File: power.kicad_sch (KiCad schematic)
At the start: 51 parts, among them CN8 POWER, U1 68000D, U10 74LS244, U11 74LS373, U12 74LS244, U13 74LS373, U2 FAT_AGNUS_8375, U32 74LS139, U34 74LS244, U35 74LS244, U36 74LS05, U37 74LS32, U5 GARY_5719, X1 XTAL

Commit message: Working on BOM
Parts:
- C1, C11, C13, C14, C2, C5, C804: MFG Part Num C412C334M5U5TA -> C440C334K5R5TA7200; Mouser (none) -> 80-C440C334K5R-TR
- C10, C12, C32, C34, C35, C36, C37, C701, C800, C801, C802, C803: MFG Part Num C410C103K1H5TAAUTO -> C410C103K1R5TA; Mouser (none) -> 80-C410C103K1R
- C811, C812, C813, C814, C815, C816: MFG Part Num EEUFR1H101 -> ECA-1VM101B; Mouser (none) -> 667-ECA-1VM101B
- C821, C822: MFG Part Num EEUFR1H470 -> ECA-1VM470B; Mouser (none) -> 667-ECA-1VM470B
- CN8: MFG Name (none) -> COMMODORE; MFG Part Num (none) -> 252167-01

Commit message: more work on BOM done
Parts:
- E101, E110: Mouser (none) -> 81-DSS1NB32A103Q91A
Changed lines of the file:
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@@
 			)
 		)
-		(property "Mouser" ""
+		(property "Mouser" " 81-DSS1NB32A103Q91A "
 			(at 109.728 104.394 90)
 			(effects
@@
 			)
 		)
-		(property "Mouser" ""
+		(property "Mouser" " 81-DSS1NB32A103Q91A "
 			(at 146.558 104.394 90)
 			(effects

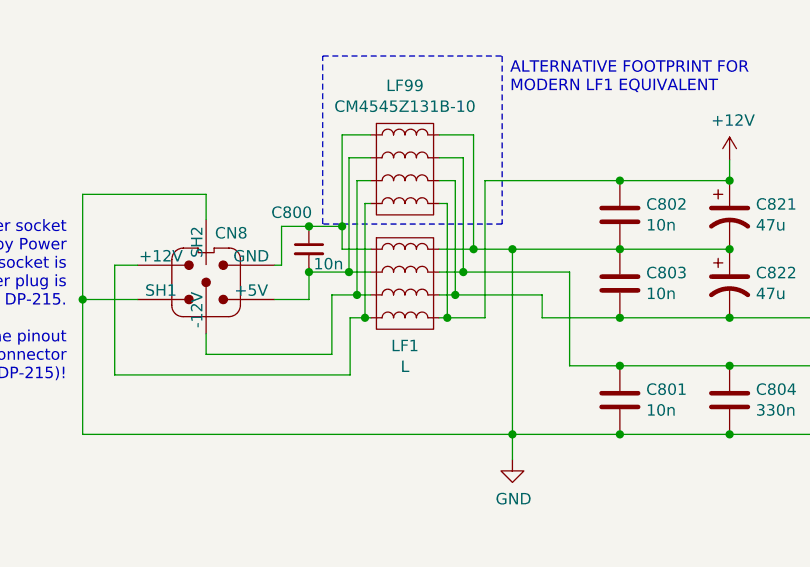
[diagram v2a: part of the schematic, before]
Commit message: More BOM work
I am marking optional components as DNP to get some overview
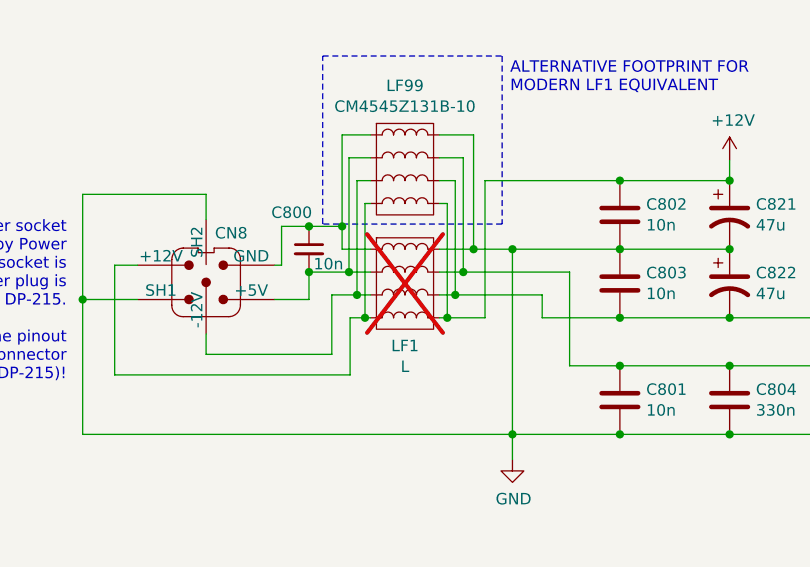
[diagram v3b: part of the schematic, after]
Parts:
- E101, E110: Mouser 81-DSS1NB32A103Q91A -> 81-DSS1NB32A103Q91A
- LF1: MFG Name (none) -> COMMODORE; now not fitted
- LF99: MFG Name (none) -> LAIRD; MFG Part Num (none) -> CM4545Z131B-10; Mouser (none) -> 875-CM4545Z131B-10
- U1: MFG Name (none) -> MOTOROLA
- U2, U5: MFG Name (none) -> COMMODORE
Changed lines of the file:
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@@
 		(in_bom yes)
 		(on_board yes)
-		(dnp no)
+		(dnp yes)
 		(property "Reference" "LF1"
 			(at 93.726 63.4492 0)
@@
 			)
 		)
+		(property "MFG Name" "COMMODORE"
+			(at 93.726 56.515 0)
+			(effects
+				(font
+					(size 1.27 1.27)
+				)
+				(hide yes)
+			)
+		)
 		(pin "4"
 		)
@@
 			)
 		)
+		(property "MFG Name" "COMMODORE"
+			(at 184.658 128.524 0)
+			(effects
+				(font
+					(size 1.27 1.27)
+				)
+				(hide yes)
+			)
+		)
 		(pin "34"
 		)
@@
 			)
 		)
+		(property "MFG Name" "MOTOROLA"
+			(at 74.168 129.794 0)
+			(effects
+				(font
+					(size 1.27 1.27)
+				)
+				(hide yes)
+			)
+		)
 		(pin "20"
 		)
@@
 			)
 		)
+		(property "MFG Name" "COMMODORE"
+			(at 112.268 127.254 0)
+			(effects
+				(font
+					(size 1.27 1.27)
+				)
+				(hide yes)
+			)
+		)
 		(pin "59"
 		)
@@
 			)
 		)
-		(property "Mouser" " 81-DSS1NB32A103Q91A "
+		(property "Mouser" "81-DSS1NB32A103Q91A "
 			(at 109.728 104.394 90)
 			(effects
@@
 			)
 		)
-		(property "Mouser" " 81-DSS1NB32A103Q91A "
+		(property "Mouser" "81-DSS1NB32A103Q91A "
 			(at 146.558 104.394 90)
 			(effects
@@
 			)
 		)
-		(property "Mouser" ""
+		(property "Mouser" "875-CM4545Z131B-10 "
+			(at 93.726 43.815 0)
+			(effects
+				(font
+					(size 1.27 1.27)
+				)
+				(hide yes)
+			)
+		)
+		(property "MFG Name" "LAIRD"
+			(at 93.726 43.815 0)
+			(effects
+				(font
+					(size 1.27 1.27)
+				)
+				(hide yes)
+			)
+		)
+		(property "MFG Part Num" "CM4545Z131B-10"
 			(at 93.726 43.815 0)
 			(effects

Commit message: BOM updates
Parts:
- U1: MFG Name MOTOROLA -> MILL-MAX; MFG Part Num (none) -> 110-93-964-41-001000; Mouser (none) -> 575-193964
- U10, U12, U35: MFG Part Num SN74LS244N -> SN74LS244N; Mouser (none) -> 595-SN74LS244N
- U11, U13: Mouser (none) -> 595-SN74LS373N
- U2: MFG Name COMMODORE -> MILL-MAX; MFG Part Num (none) -> 940-44-084-24-000000; Mouser (none) -> 575-948424
- U32: MFG Part Num SN74LS139AN -> SN74LS139AN; Mouser (none) -> 595-SN74LS139AN
- U34: MFG Name (none) -> TI; MFG Part Num (none) -> SN74LS244N; Mouser (none) -> 595-SN74LS244N
- U36: MFG Part Num SN74LS05N -> SN74LS05N; Mouser (none) -> 595-SN74LS05N
- U37: MFG Part Num SN74LS32N -> SN74LS32N; Mouser (none) -> 595-SN74LS32N
- U5: MFG Name COMMODORE -> 3M; MFG Part Num (none) -> 4848-6000-CP; Mouser (none) -> 517-4848-6000-CP
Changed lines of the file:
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@@
 			)
 		)
-		(property "MFG Part Num" "SN74LS32N"
+		(property "MFG Part Num" "SN74LS32N "
 			(at 217.678 179.324 0)
 			(effects
@@
 			)
 		)
-		(property "Mouser" ""
+		(property "Mouser" "595-SN74LS32N "
 			(at 217.678 179.324 0)
 			(effects
@@
 			)
 		)
-		(property "Mouser" ""
+		(property "Mouser" "517-4848-6000-CP "
+			(at 184.658 128.524 0)
+			(effects
+				(font
+					(size 1.27 1.27)
+				)
+				(hide yes)
+			)
+		)
+		(property "MFG Name" "3M"
 			(at 184.658 128.524 0)
 			(effects
@@
 			)
 		)
-		(property "MFG Name" "COMMODORE"
+		(property "MFG Part Num" "4848-6000-CP "
 			(at 184.658 128.524 0)
 			(effects
@@
 			)
 		)
-		(property "Mouser" ""
+		(property "Mouser" "575-193964 "
 			(at 74.168 129.794 0)
 			(effects
@@
 			)
 		)
-		(property "MFG Name" "MOTOROLA"
+		(property "MFG Name" "MILL-MAX"
+			(at 74.168 129.794 0)
+			(effects
+				(font
+					(size 1.27 1.27)
+				)
+				(hide yes)
+			)
+		)
+		(property "MFG Part Num" "110-93-964-41-001000"
 			(at 74.168 129.794 0)
 			(effects
@@
 			)
 		)
-		(property "Mouser" ""
+		(property "Mouser" "575-948424 "
 			(at 112.268 127.254 0)
 			(effects
@@
 			)
 		)
-		(property "MFG Name" "COMMODORE"
+		(property "MFG Name" "MILL-MAX"
+			(at 112.268 127.254 0)
+			(effects
+				(font
+					(size 1.27 1.27)
+				)
+				(hide yes)
+			)
+		)
+		(property "MFG Part Num" "940-44-084-24-000000 "
 			(at 112.268 127.254 0)
 			(effects
@@
 			)
 		)
-		(property "Mouser" ""
+		(property "Mouser" "595-SN74LS373N "
 			(at 72.898 236.474 0)
 			(effects
@@
 			)
 		)
-		(property "Mouser" ""
+		(property "Mouser" "595-SN74LS373N "
 			(at 145.288 236.474 0)
 			(effects
@@
 			)
 		)
-		(property "MFG Part Num" "SN74LS244N"
+		(property "MFG Part Num" "SN74LS244N "
 			(at 34.798 235.204 0)
 			(effects
@@
 			)
 		)
-		(property "Mouser" ""
+		(property "Mouser" "595-SN74LS244N "
 			(at 34.798 235.204 0)
 			(effects
@@
 			)
 		)
-		(property "MFG Part Num" "SN74LS244N"
+		(property "MFG Part Num" "SN74LS244N "
 			(at 107.188 235.204 0)
 			(effects
@@
 			)
 		)
-		(property "Mouser" ""
+		(property "Mouser" "595-SN74LS244N "
 			(at 107.188 235.204 0)
 			(effects
@@
 			)
 		)
-		(property "MFG Part Num" "SN74LS139AN"
+		(property "MFG Part Num" "SN74LS139AN "
 			(at 58.928 179.324 0)
 			(effects
@@
 			)
 		)
-		(property "Mouser" ""
+		(property "Mouser" "595-SN74LS139AN "
 			(at 58.928 179.324 0)
 			(effects
@@
 			)
 		)
-		(property "MFG Part Num" "SN74LS244N"
+		(property "MFG Part Num" "SN74LS244N "
 			(at 133.858 179.324 0)
 			(effects
@@
 			)
 		)
-		(property "Mouser" ""
+		(property "Mouser" "595-SN74LS244N "
 			(at 133.858 179.324 0)
 			(effects
@@
 			)
 		)
-		(property "MFG Part Num" "SN74LS05N"
+		(property "MFG Part Num" "SN74LS05N "
 			(at 174.498 179.324 0)
 			(effects
@@
 			)
 		)
-		(property "Mouser" ""
+		(property "Mouser" "595-SN74LS05N "
 			(at 174.498 179.324 0)
 			(effects
@@
 			)
 		)
-		(property "Mouser" ""
+		(property "Mouser" "595-SN74LS244N "
+			(at 97.028 179.324 0)
+			(effects
+				(font
+					(size 1.27 1.27)
+				)
+				(hide yes)
+			)
+		)
+		(property "MFG Name" "TI"
+			(at 97.028 179.324 0)
+			(effects
+				(font
+					(size 1.27 1.27)
+				)
+				(hide yes)
+			)
+		)
+		(property "MFG Part Num" "SN74LS244N "
 			(at 97.028 179.324 0)
 			(effects

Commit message: even  more BOM work
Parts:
- U32: value 74LS139 -> 74F139; MFG Part Num SN74LS139AN -> CD74ACT139E; Mouser 595-SN74LS139AN -> 595-CD74ACT139E
- U34, U35: value 74LS244 -> 74F244; MFG Part Num SN74LS244N -> (none); Mouser 595-SN74LS244N -> (none)
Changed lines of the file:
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@@
 			)
 		)
-		(property "Value" "74LS139"
+		(property "Value" "74F139"
 			(at 61.468 189.484 0)
 			(effects
@@
 			)
 		)
-		(property "MFG Part Num" "SN74LS139AN "
+		(property "MFG Part Num" "CD74ACT139E "
 			(at 58.928 179.324 0)
 			(effects
@@
 			)
 		)
-		(property "Mouser" "595-SN74LS139AN "
+		(property "Mouser" "595-CD74ACT139E "
 			(at 58.928 179.324 0)
 			(effects
@@
 			)
 		)
-		(property "Value" "74LS244"
+		(property "Value" "74F244"
 			(at 136.398 188.214 0)
 			(effects
@@
 			)
 		)
-		(property "MFG Part Num" "SN74LS244N "
+		(property "MFG Part Num" ""
 			(at 133.858 179.324 0)
 			(effects
@@
 			)
 		)
-		(property "Mouser" "595-SN74LS244N "
+		(property "Mouser" ""
 			(at 133.858 179.324 0)
 			(effects
@@
 			)
 		)
-		(property "Value" "74LS244"
+		(property "Value" "74F244"
 			(at 98.425 187.96 0)
 			(effects
@@
 			)
 		)
-		(property "Mouser" "595-SN74LS244N "
+		(property "Mouser" ""
 			(at 97.028 179.324 0)
 			(effects
@@
 			)
 		)
-		(property "MFG Part Num" "SN74LS244N "
+		(property "MFG Part Num" ""
 			(at 97.028 179.324 0)
 			(effects

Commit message: added mouser part numbers
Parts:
- U34, U35: MFG Part Num (none) -> SN74F244N; Mouser (none) -> 595-SN74F244N
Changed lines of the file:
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@@
 			)
 		)
-		(property "MFG Part Num" ""
+		(property "MFG Part Num" "SN74F244N "
 			(at 133.858 179.324 0)
 			(effects
@@
 			)
 		)
-		(property "Mouser" ""
+		(property "Mouser" "595-SN74F244N "
 			(at 133.858 179.324 0)
 			(effects
@@
 			)
 		)
-		(property "Mouser" ""
+		(property "Mouser" "595-SN74F244N "
 			(at 97.028 179.324 0)
 			(effects
@@
 			)
 		)
-		(property "MFG Part Num" ""
+		(property "MFG Part Num" "SN74F244N "
 			(at 97.028 179.324 0)
 			(effects

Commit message: more silkscreen work
removed sockets for standard IC's
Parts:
- U10, U11, U12, U13: footprint Package_DIP:DIP-20_W7.62mm_Socket_LongPads -> Package_DIP:DIP-20_W7.62mm_LongPads
- U36, U37: footprint Package_DIP:DIP-14_W7.62mm_Socket_LongPads -> Package_DIP:DIP-14_W7.62mm_LongPads
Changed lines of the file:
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@@
 	(title_block
 		(title "Rämixx500_max")
-		(date "2026-04-09")
+		(date "2026-04-26")
 		(rev "3")
 		(company "SukkoPera")
@@
 			)
 		)
-		(property "Footprint" "Package_DIP:DIP-14_W7.62mm_Socket_LongPads"
+		(property "Footprint" "Package_DIP:DIP-14_W7.62mm_LongPads"
 			(at 217.678 179.324 0)
 			(effects
@@
 			)
 		)
-		(property "Footprint" "Package_DIP:DIP-20_W7.62mm_Socket_LongPads"
+		(property "Footprint" "Package_DIP:DIP-20_W7.62mm_LongPads"
 			(at 72.898 236.474 0)
 			(effects
@@
 			)
 		)
-		(property "Footprint" "Package_DIP:DIP-20_W7.62mm_Socket_LongPads"
+		(property "Footprint" "Package_DIP:DIP-20_W7.62mm_LongPads"
 			(at 145.288 236.474 0)
 			(effects
@@
 			)
 		)
-		(property "Footprint" "Package_DIP:DIP-20_W7.62mm_Socket_LongPads"
+		(property "Footprint" "Package_DIP:DIP-20_W7.62mm_LongPads"
 			(at 34.798 235.204 0)
 			(effects
@@
 			)
 		)
-		(property "Footprint" "Package_DIP:DIP-20_W7.62mm_Socket_LongPads"
+		(property "Footprint" "Package_DIP:DIP-20_W7.62mm_LongPads"
 			(at 107.188 235.204 0)
 			(effects
@@
 			)
 		)
-		(property "Footprint" "Package_DIP:DIP-14_W7.62mm_Socket_LongPads"
+		(property "Footprint" "Package_DIP:DIP-14_W7.62mm_LongPads"
 			(at 174.498 179.324 0)
 			(effects
